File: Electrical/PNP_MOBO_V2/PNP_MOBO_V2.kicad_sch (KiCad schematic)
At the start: 47 parts, among them J1 USB_C_Receptacle_USB2.0_16P, J2 Screw_Terminal_01x02, J4 Conn_01x03_Pin, J6 Conn_01x03_Pin, SW1 SW_Push, SW2 SW_Push, U1 ESP32-S3-WROOM-1, U3 SN65HVD230, U4 AMS1117-3.3

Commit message: circuit mostly done!
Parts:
- J2: footprint Connector_Molex:Molex_KK-396_A-41792-0002_1x02_P3.96mm_Horizontal -> Connector_BarrelJack:BarrelJack_SwitchcraftConxall_RAPC10U_Horizontal
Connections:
- net GPIO3: now also R36.1
- net GPIO1 renamed P_1_DATA
- net GPIO10 renamed DRIVE_YAW_DIR
- net DRIVE_YAW_DIR: no longer R36.1
- net GPIO11 renamed DRIVE_YAW_STP
- net GPIO12 renamed SW_PUMP
- net GPIO13 renamed SW_V1
- net GPIO14 renamed SW_V2
- net GPIO15 renamed DRIVE_Y_DIR
- net GPIO16 renamed LIM_Y
- net GPIO17 renamed DRIVE_Z_DIR
- net GPIO18 renamed DRIVE_Z_STP
- net GPIO2 renamed P_1_CLK
- net GPIO4 renamed DRIVE_X_DIR
- net GPIO41 renamed P_2_DATA
- net GPIO42 renamed P_2_CLK
- net GPIO5 renamed DRIVE_X_STP
- net GPIO6 renamed LIM_X
- net GPIO7 renamed DRIVE_Y_STP
- net SCL renamed DRIVE_EN
- net SDA renamed LIM_Z
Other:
- moved on the sheet: J4

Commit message: wip pcbv2
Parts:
- removed J2: Screw_Terminal_01x02, Connector_BarrelJack:BarrelJack_SwitchcraftConxall_RAPC10U_Horizontal, symbol Connector:Screw_Terminal_01x02
- added J8: Barrel_Jack_MountingPin, Connector_BarrelJack:BarrelJack_CUI_PJ-063AH_Horizontal, symbol Connector:Barrel_Jack_MountingPin
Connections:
- net 12V: now also J8.1
- net GND: now also J8.2
- net GPIO38: now also U3.4 (R)
- net GPIO39: now also U3.1 (D)
- net GPIO47: no longer U3.4 (R)
- net GPIO48: no longer U3.1 (D)
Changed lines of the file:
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@@
 	)
 	(junction
-		(at 39.37 151.13)
-		(diameter 0)
-		(color 0 0 0 0)
-	)
-	(junction
 		(at 247.65 34.29)
 		(diameter 0)
@@
 	)
 	(junction
+		(at 39.37 151.13)
+		(diameter 0)
+		(color 0 0 0 0)
+	)
+	(junction
 		(at 229.87 41.91)
 		(diameter 0)
@@
 	(wire
 		(pts
+			(xy 54.61 143.51) (xy 52.07 143.51)
+		)
+		(stroke
+			(width 0)
+			(type default)
+		)
+	)
+	(wire
+		(pts
 			(xy 142.24 154.94) (xy 142.24 157.48)
 		)
@@
 	(wire
 		(pts
-			(xy 27.94 160.02) (xy 25.4 160.02)
+			(xy 39.37 151.13) (xy 54.61 151.13)
 		)
 		(stroke
@@
 	(wire
 		(pts
-			(xy 146.05 173.99) (xy 146.05 170.18)
+			(xy 27.94 160.02) (xy 25.4 160.02)
 		)
 		(stroke
@@
 	(wire
 		(pts
-			(xy 176.53 66.04) (xy 189.23 66.04)
+			(xy 146.05 173.99) (xy 146.05 170.18)
 		)
 		(stroke
@@
 	(wire
 		(pts
-			(xy 133.35 78.74) (xy 146.05 78.74)
+			(xy 176.53 66.04) (xy 189.23 66.04)
 		)
 		(stroke
@@
 	(wire
 		(pts
-			(xy 39.37 151.13) (xy 41.91 151.13)
+			(xy 133.35 78.74) (xy 146.05 78.74)
 		)
 		(stroke
@@
 	(wire
 		(pts
+			(xy 54.61 146.05) (xy 54.61 143.51)
+		)
+		(stroke
+			(width 0)
+			(type default)
+		)
+	)
+	(wire
+		(pts
 			(xy 229.87 20.32) (xy 229.87 29.21)
 		)
@@
 		)
 	)
-	(label "GPIO47"
+	(label "GPIO38"
 		(at 209.55 135.89 0)
 		(effects
@@
 		)
 	)
-	(label "GPIO48"
+	(label "GPIO39"
 		(at 209.55 133.35 0)
 		(effects
@@
 	)
 	(symbol
+		(lib_id "Connector:Barrel_Jack_MountingPin")
+		(at 62.23 148.59 180)
+		(unit 1)
+		(exclude_from_sim no)
+		(in_bom yes)
+		(on_board yes)
+		(dnp no)
+		(fields_autoplaced yes)
+		(property "Reference" "J8"
+			(at 68.58 146.9643 0)
+			(effects
+				(font
+					(size 1.27 1.27)
+				)
+				(justify right)
+			)
+		)
+		(property "Value" "Barrel_Jack_MountingPin"
+			(at 68.58 149.5043 0)
+			(effects
+				(font
+					(size 1.27 1.27)
+				)
+				(justify right)
+			)
+		)
+		(property "Footprint" "Connector_BarrelJack:BarrelJack_CUI_PJ-063AH_Horizontal"
+			(at 60.96 147.574 0)
+			(effects
+				(font
+					(size 1.27 1.27)
+				)
+				(hide yes)
+			)
+		)
+		(property "Datasheet" "~"
+			(at 60.96 147.574 0)
+			(effects
+				(font
+					(size 1.27 1.27)
+				)
+				(hide yes)
+			)
+		)
+		(property "Description" "DC Barrel Jack with a mounting pin"
+			(at 62.23 148.59 0)
+			(effects
+				(font
+					(size 1.27 1.27)
+				)
+				(hide yes)
+			)
+		)
+		(pin "2"
+		)
+		(pin "MP"
+		)
+		(pin "1"
+		)
+		(instances
+			(project ""
+				(path "/cdf8736a-c168-4946-980b-ea20704015fc"
+					(reference "J8")
+					(unit 1)
+				)
+			)
+		)
+	)
+	(symbol
 		(lib_id "Device:R")
 		(at 229.87 33.02 0)
@@
 		(on_board yes)
 		(dnp no)
-		(fields_autoplaced yes)
 		(property "Reference" "TP1"
-			(at 41.91 146.5579 0)
+			(at 41.148 143.764 0)
 			(effects
 				(font
@@
 		)
 		(property "Value" "TestPoint"
-			(at 41.91 149.0979 0)
+			(at 41.148 147.32 0)
 			(effects
 				(font
@@
 	(symbol
 		(lib_id "power:GND")
-		(at 41.91 153.67 0)
+		(at 52.07 143.51 0)
 		(unit 1)
 		(exclude_from_sim no)
@@
 		(dnp no)
 		(property "Reference" "#PWR05"
-			(at 41.91 160.02 0)
+			(at 52.07 149.86 0)
 			(effects
 				(font
@@
 		)
 		(property "Value" "GND"
-			(at 45.974 157.226 0)
+			(at 49.53 142.494 0)
 			(effects
 				(font
@@
 		)
 		(property "Footprint" ""
-			(at 41.91 153.67 0)
+			(at 52.07 143.51 0)
 			(effects
 				(font
@@
 		)
 		(property "Datasheet" ""
-			(at 41.91 153.67 0)
+			(at 52.07 143.51 0)
 			(effects
 				(font
@@
 		)
 		(property "Description" "Power symbol creates a global label with name \"GND\" , ground"
-			(at 41.91 153.67 0)
+			(at 52.07 143.51 0)
 			(effects
 				(font
@@
 					(unit 1)
 				)
-			)
-		)
-	)
-	(symbol
-		(lib_id "Connector:Screw_Terminal_01x02")
-		(at 46.99 151.13 0)
-		(unit 1)
-		(exclude_from_sim no)
-		(in_bom yes)
-		(on_board yes)
-		(dnp no)
-		(property "Reference" "J2"
-			(at 49.53 151.1299 0)
-			(effects
-				(font
-					(size 1.27 1.27)
-				)
-				(justify left)
-			)
-		)
-		(property "Value" "Screw_Terminal_01x02"
-			(at 53.594 159.766 0)
-			(effects
-				(font
-					(size 1.27 1.27)
-				)
-				(justify left)
-				(hide yes)
-			)
-		)
-		(property "Footprint" "Connector_BarrelJack:BarrelJack_SwitchcraftConxall_RAPC10U_Horizontal"
-			(at 46.99 151.13 0)
-			(effects
-				(font
-					(size 1.27 1.27)
-				)
-				(hide yes)
-			)
-		)
-		(property "Datasheet" "~"
-			(at 46.99 151.13 0)
-			(effects
-				(font
-					(size 1.27 1.27)
-				)
-				(hide yes)
-			)
-		)
-		(property "Description" "Generic screw terminal, single row, 01x02, script generated (kicad-library-utils/schlib/autogen/connector/)"
-			(at 46.99 151.13 0)
-			(effects
-				(font
-					(size 1.27 1.27)
-				)
-				(hide yes)
-			)
-		)
-		(pin "2"
-		)
-		(pin "1"
-		)
-		(instances
-			(project ""
-				(path "/cdf8736a-c168-4946-980b-ea20704015fc"
-					(reference "J2")
-					(unit 1)
-				)

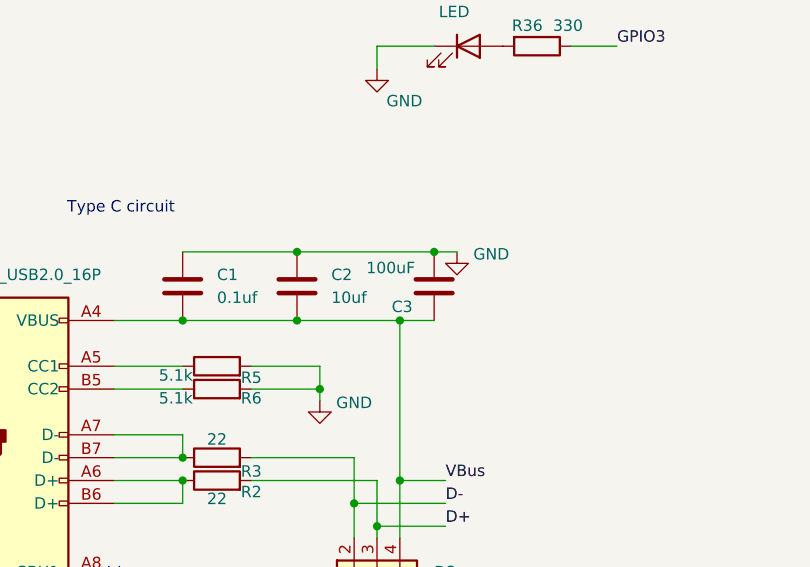
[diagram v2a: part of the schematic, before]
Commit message: rooting done, only last check and test missing
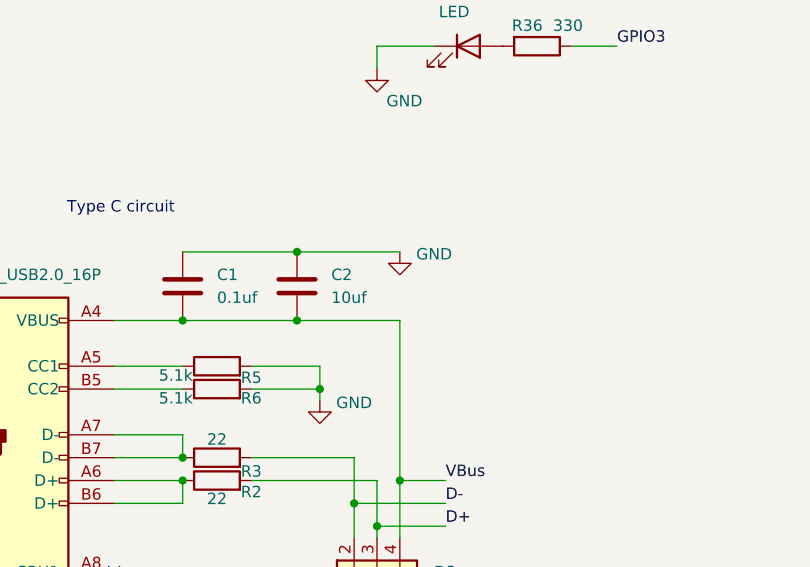
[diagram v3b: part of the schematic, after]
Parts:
- removed C3: 100uF, Capacitor_SMD:CP_Elec_8x10, symbol Device:C
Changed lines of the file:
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@@
 	)
 	(junction
-		(at 154.94 142.24)
-		(diameter 0)
-		(color 0 0 0 0)
-	)
-	(junction
 		(at 139.7 142.24)
 		(diameter 0)
@@
 	)
 	(junction
-		(at 151.13 149.86)
-		(diameter 0)
-		(color 0 0 0 0)
-	)
-	(junction
 		(at 22.86 176.53)
 		(diameter 0)
@@
 	(wire
 		(pts
-			(xy 154.94 142.24) (xy 157.48 142.24)
+			(xy 139.7 142.24) (xy 151.13 142.24)
 		)
 		(stroke
@@
 	(wire
 		(pts
-			(xy 139.7 142.24) (xy 154.94 142.24)
-		)
-		(stroke
-			(width 0)
-			(type default)
-		)
-	)
-	(wire
-		(pts
 			(xy 119.38 162.56) (xy 127 162.56)
 		)
@@
 	(wire
 		(pts
-			(xy 151.13 149.86) (xy 154.94 149.86)
-		)
-		(stroke
-			(width 0)
-			(type default)
-		)
-	)
-	(wire
-		(pts
 			(xy 251.46 49.53) (xy 247.65 49.53)
 		)
@@
 	)
 	(symbol
-		(lib_id "Device:C")
-		(at 154.94 146.05 0)
-		(unit 1)
-		(exclude_from_sim no)
-		(in_bom yes)
-		(on_board yes)
-		(dnp no)
-		(property "Reference" "C3"
-			(at 151.384 148.336 0)
-			(effects
-				(font
-					(size 1.27 1.27)
-				)
-			)
-		)
-		(property "Value" "100uF"
-			(at 150.114 144.018 0)
-			(effects
-				(font
-					(size 1.27 1.27)
-				)
-			)
-		)
-		(property "Footprint" "Capacitor_SMD:CP_Elec_8x10"
-			(at 155.9052 149.86 0)
-			(effects
-				(font
-					(size 1.27 1.27)
-				)
-				(hide yes)
-			)
-		)
-		(property "Datasheet" "~"
-			(at 154.94 146.05 0)
-			(effects
-				(font
-					(size 1.27 1.27)
-				)
-				(hide yes)
-			)
-		)
-		(property "Description" "Unpolarized capacitor"
-			(at 154.94 146.05 0)
-			(effects
-				(font
-					(size 1.27 1.27)
-				)
-				(hide yes)
-			)
-		)
-		(pin "1"
-		)
-		(pin "2"
-		)
-		(instances
-			(project "PNP_MOBO_V2"
-				(path "/cdf8736a-c168-4946-980b-ea20704015fc"
-					(reference "C3")
-					(unit 1)
-				)
-			)
-		)
-	)
-	(symbol
 		(lib_id "Device:R")
 		(at 130.81 157.48 90)
@@
 	(symbol
 		(lib_id "power:GND")
-		(at 157.48 142.24 0)
+		(at 151.13 142.24 0)
 		(unit 1)
 		(exclude_from_sim no)
@@
 		(dnp no)
 		(property "Reference" "#PWR03"
-			(at 157.48 148.59 0)
+			(at 151.13 148.59 0)
 			(effects
 				(font
@@
 		)
 		(property "Value" "GND"
-			(at 161.29 142.494 0)
+			(at 154.94 142.494 0)
 			(effects
 				(font
@@
 		)
 		(property "Footprint" ""
-			(at 157.48 142.24 0)
+			(at 151.13 142.24 0)
 			(effects
 				(font
@@
 		)
 		(property "Datasheet" ""
-			(at 157.48 142.24 0)
+			(at 151.13 142.24 0)
 			(effects
 				(font
@@
 		)
 		(property "Description" "Power symbol creates a global label with name \"GND\" , ground"
-			(at 157.48 142.24 0)
+			(at 151.13 142.24 0)
 			(effects
 				(font

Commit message: add i bom and fabrication file
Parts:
- added REF1, REF2: Conn_01x01_Pin, Connector_PinHeader_1.00mm:PinHeader_1x01_P1.00mm_Vertical, symbol Connector:Conn_01x01_Pin
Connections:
- no-connect marks 3 -> 5
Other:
- note added: "REF 1 and REF 2"
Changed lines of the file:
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@@
 		)
 	)
+	(text "REF 1 and REF 2"
+		(exclude_from_sim no)
+		(at 112.776 94.742 0)
+		(effects
+			(font
+				(size 1.27 1.27)
+			)
+		)
+	)
 	(text "ESP32 Circuit\n\n"
 		(exclude_from_sim no)
@@
 	)
 	(no_connect
+		(at 116.84 110.49)
+	)
+	(no_connect
 		(at 119.38 180.34)
 	)
 	(no_connect
+		(at 116.84 102.87)
+	)
+	(no_connect
 		(at 217.17 138.43)
 	)
@@
 	)
 	(symbol
+		(lib_id "Connector:Conn_01x01_Pin")
+		(at 111.76 102.87 0)
+		(unit 1)
+		(exclude_from_sim no)
+		(in_bom yes)
+		(on_board yes)
+		(dnp no)
+		(fields_autoplaced yes)
+		(property "Reference" "REF1"
+			(at 112.395 97.79 0)
+			(effects
+				(font
+					(size 1.27 1.27)
+				)
+			)
+		)
+		(property "Value" "Conn_01x01_Pin"
+			(at 112.395 100.33 0)
+			(effects
+				(font
+					(size 1.27 1.27)
+				)
+			)
+		)
+		(property "Footprint" "Connector_PinHeader_1.00mm:PinHeader_1x01_P1.00mm_Vertical"
+			(at 111.76 102.87 0)
+			(effects
+				(font
+					(size 1.27 1.27)
+				)
+				(hide yes)
+			)
+		)
+		(property "Datasheet" "~"
+			(at 111.76 102.87 0)
+			(effects
+				(font
+					(size 1.27 1.27)
+				)
+				(hide yes)
+			)
+		)
+		(property "Description" "Generic connector, single row, 01x01, script generated"
+			(at 111.76 102.87 0)
+			(effects
+				(font
+					(size 1.27 1.27)
+				)
+				(hide yes)
+			)
+		)
+		(pin "1"
+		)
+		(instances
+			(project ""
+				(path "/cdf8736a-c168-4946-980b-ea20704015fc"
+					(reference "REF1")
+					(unit 1)
+				)
+			)
+		)
+	)
+	(symbol
 		(lib_id "Connector:TestPoint")
 		(at 262.89 24.13 0)
@@
 					(unit 1)
 				)
+			)
+		)
+	)
+	(symbol
+		(lib_id "Connector:Conn_01x01_Pin")
+		(at 111.76 110.49 0)
+		(unit 1)
+		(exclude_from_sim no)
+		(in_bom yes)
+		(on_board yes)
+		(dnp no)
+		(fields_autoplaced yes)
+		(property "Reference" "REF2"
+			(at 112.395 105.41 0)
+			(effects
+				(font
+					(size 1.27 1.27)
+				)
+			)
+		)
+		(property "Value" "Conn_01x01_Pin"
+			(at 112.395 107.95 0)
+			(effects
+				(font
+					(size 1.27 1.27)
+				)
+			)
+		)
+		(property "Footprint" "Connector_PinHeader_1.00mm:PinHeader_1x01_P1.00mm_Vertical"
+			(at 111.76 110.49 0)
+			(effects
+				(font
+					(size 1.27 1.27)
+				)
+				(hide yes)
+			)
+		)
+		(property "Datasheet" "~"
+			(at 111.76 110.49 0)
+			(effects
+				(font
+					(size 1.27 1.27)
+				)
+				(hide yes)
+			)
+		)
+		(property "Description" "Generic connector, single row, 01x01, script generated"
+			(at 111.76 110.49 0)
+			(effects
+				(font
+					(size 1.27 1.27)
+				)
+				(hide yes)
+			)
+		)
+		(pin "1"
+		)
+		(instances
+			(project "PNP_MOBO_V2"
+				(path "/cdf8736a-c168-4946-980b-ea20704015fc"
+					(reference "REF2")
+					(unit 1)
+				)

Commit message: fix: last change before order
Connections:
- net 12V: now also J8.2; no longer J8.1
- net GND: now also J8.1; no longer J8.2
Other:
- moved on the sheet: J8
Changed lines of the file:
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@@
 	)
 	(junction
+		(at 39.37 151.13)
+		(diameter 0)
+		(color 0 0 0 0)
+	)
+	(junction
 		(at 60.96 184.15)
 		(diameter 0)
@@
 	)
 	(junction
-		(at 39.37 151.13)
-		(diameter 0)
-		(color 0 0 0 0)
-	)
-	(junction
 		(at 229.87 41.91)
 		(diameter 0)
@@
 	(wire
 		(pts
-			(xy 54.61 143.51) (xy 52.07 143.51)
+			(xy 54.61 156.21) (xy 52.07 156.21)
 		)
 		(stroke
@@
 	(wire
 		(pts
-			(xy 39.37 151.13) (xy 54.61 151.13)
-		)
-		(stroke
-			(width 0)
-			(type default)
-		)
-	)
-	(wire
-		(pts
 			(xy 27.94 160.02) (xy 25.4 160.02)
 		)
@@
 	(wire
 		(pts
-			(xy 54.61 146.05) (xy 54.61 143.51)
-		)
-		(stroke
-			(width 0)
-			(type default)
-		)
-	)
-	(wire
-		(pts
 			(xy 229.87 20.32) (xy 229.87 29.21)
 		)
@@
 	(wire
 		(pts
+			(xy 39.37 151.13) (xy 54.61 151.13)
+		)
+		(stroke
+			(width 0)
+			(type default)
+		)
+	)
+	(wire
+		(pts
 			(xy 134.62 167.64) (xy 148.59 167.64)
 		)
@@
 	(symbol
 		(lib_id "Connector:Barrel_Jack_MountingPin")
-		(at 62.23 148.59 180)
+		(at 62.23 153.67 180)
 		(unit 1)
 		(exclude_from_sim no)
@@
 		(fields_autoplaced yes)
 		(property "Reference" "J8"
-			(at 68.58 146.9643 0)
+			(at 68.58 152.0443 0)
 			(effects
 				(font
@@
 		)
 		(property "Value" "Barrel_Jack_MountingPin"
-			(at 68.58 149.5043 0)
+			(at 68.58 154.5843 0)
 			(effects
 				(font
@@
 		)
 		(property "Footprint" "Connector_BarrelJack:BarrelJack_CUI_PJ-063AH_Horizontal"
-			(at 60.96 147.574 0)
+			(at 60.96 152.654 0)
 			(effects
 				(font
@@
 		)
 		(property "Datasheet" "~"
-			(at 60.96 147.574 0)
+			(at 60.96 152.654 0)
 			(effects
 				(font
@@
 		)
 		(property "Description" "DC Barrel Jack with a mounting pin"
-			(at 62.23 148.59 0)
+			(at 62.23 153.67 0)
 			(effects
 				(font
@@
 	(symbol
 		(lib_id "power:GND")
-		(at 52.07 143.51 0)
+		(at 52.07 156.21 0)
 		(unit 1)
 		(exclude_from_sim no)
@@
 		(dnp no)
 		(property "Reference" "#PWR05"
-			(at 52.07 149.86 0)
+			(at 52.07 162.56 0)
 			(effects
 				(font
@@
 		)
 		(property "Value" "GND"
-			(at 49.53 142.494 0)
+			(at 49.53 155.194 0)
 			(effects
 				(font
@@
 		)
 		(property "Footprint" ""
-			(at 52.07 143.51 0)
+			(at 52.07 156.21 0)
 			(effects
 				(font
@@
 		)
 		(property "Datasheet" ""
-			(at 52.07 143.51 0)
+			(at 52.07 156.21 0)
 			(effects
 				(font
@@
 		)
 		(property "Description" "Power symbol creates a global label with name \"GND\" , ground"
-			(at 52.07 143.51 0)
+			(at 52.07 156.21 0)
 			(effects
 				(font

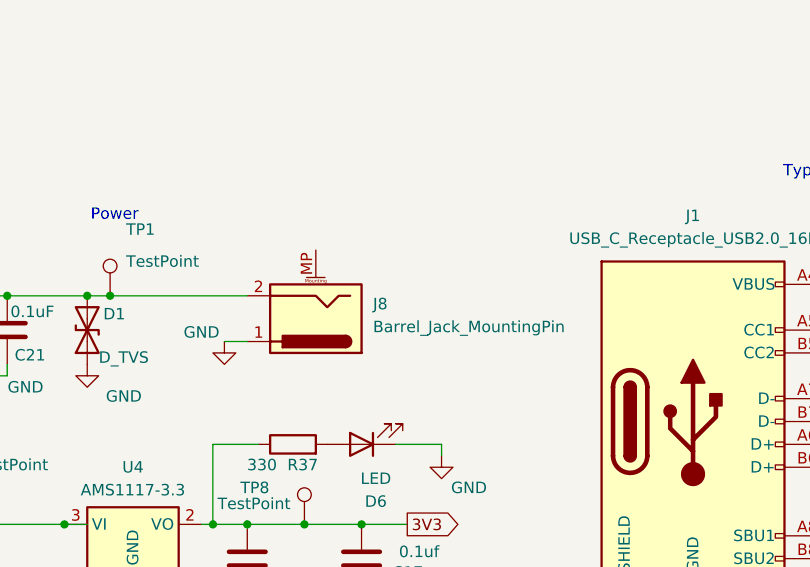
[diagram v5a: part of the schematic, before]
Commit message: fix: wrong connection on power inpt
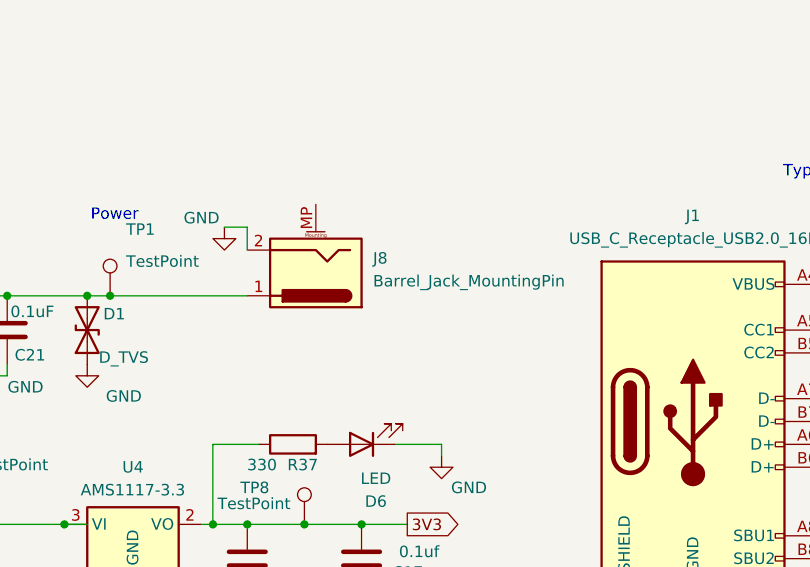
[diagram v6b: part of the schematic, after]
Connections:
- net 12V: now also J8.1; no longer J8.2
- net GND: now also J8.2; no longer J8.1
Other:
- moved on the sheet: J8
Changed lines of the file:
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@@
 	)
 	(junction
-		(at 39.37 151.13)
-		(diameter 0)
-		(color 0 0 0 0)
-	)
-	(junction
 		(at 60.96 184.15)
 		(diameter 0)
@@
 	)
 	(junction
+		(at 39.37 151.13)
+		(diameter 0)
+		(color 0 0 0 0)
+	)
+	(junction
 		(at 229.87 41.91)
 		(diameter 0)
@@
 	(wire
 		(pts
-			(xy 54.61 156.21) (xy 52.07 156.21)
+			(xy 54.61 143.51) (xy 52.07 143.51)
 		)
 		(stroke
@@
 	(wire
 		(pts
+			(xy 39.37 151.13) (xy 54.61 151.13)
+		)
+		(stroke
+			(width 0)
+			(type default)
+		)
+	)
+	(wire
+		(pts
 			(xy 27.94 160.02) (xy 25.4 160.02)
 		)
@@
 	(wire
 		(pts
+			(xy 54.61 146.05) (xy 54.61 143.51)
+		)
+		(stroke
+			(width 0)
+			(type default)
+		)
+	)
+	(wire
+		(pts
 			(xy 229.87 20.32) (xy 229.87 29.21)
 		)
@@
 	(wire
 		(pts
-			(xy 39.37 151.13) (xy 54.61 151.13)
-		)
-		(stroke
-			(width 0)
-			(type default)
-		)
-	)
-	(wire
-		(pts
 			(xy 134.62 167.64) (xy 148.59 167.64)
 		)
@@
 	(symbol
 		(lib_id "Connector:Barrel_Jack_MountingPin")
-		(at 62.23 153.67 180)
+		(at 62.23 148.59 180)
 		(unit 1)
 		(exclude_from_sim no)
@@
 		(fields_autoplaced yes)
 		(property "Reference" "J8"
-			(at 68.58 152.0443 0)
+			(at 68.58 146.9643 0)
 			(effects
 				(font
@@
 		)
 		(property "Value" "Barrel_Jack_MountingPin"
-			(at 68.58 154.5843 0)
+			(at 68.58 149.5043 0)
 			(effects
 				(font
@@
 		)
 		(property "Footprint" "Connector_BarrelJack:BarrelJack_CUI_PJ-063AH_Horizontal"
-			(at 60.96 152.654 0)
+			(at 60.96 147.574 0)
 			(effects
 				(font
@@
 		)
 		(property "Datasheet" "~"
-			(at 60.96 152.654 0)
+			(at 60.96 147.574 0)
 			(effects
 				(font
@@
 		)
 		(property "Description" "DC Barrel Jack with a mounting pin"
-			(at 62.23 153.67 0)
+			(at 62.23 148.59 0)
 			(effects
 				(font
@@
 	(symbol
 		(lib_id "power:GND")
-		(at 52.07 156.21 0)
+		(at 52.07 143.51 0)
 		(unit 1)
 		(exclude_from_sim no)
@@
 		(dnp no)
 		(property "Reference" "#PWR05"
-			(at 52.07 162.56 0)
+			(at 52.07 149.86 0)
 			(effects
 				(font
@@
 		)
 		(property "Value" "GND"
-			(at 49.53 155.194 0)
+			(at 49.53 142.494 0)
 			(effects
 				(font
@@
 		)
 		(property "Footprint" ""
-			(at 52.07 156.21 0)
+			(at 52.07 143.51 0)
 			(effects
 				(font
@@
 		)
 		(property "Datasheet" ""
-			(at 52.07 156.21 0)
+			(at 52.07 143.51 0)
 			(effects
 				(font
@@
 		)
 		(property "Description" "Power symbol creates a global label with name \"GND\" , ground"
-			(at 52.07 156.21 0)
+			(at 52.07 143.51 0)
 			(effects
 				(font
